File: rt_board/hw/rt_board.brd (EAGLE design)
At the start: 100 x 80 mm, 23 parts, among them IC1 MCP170333MB, IC2 FT232RL, Q1 8MHz, U1 STM32F051R8T7, X1 PWR, X2 MINI-USB

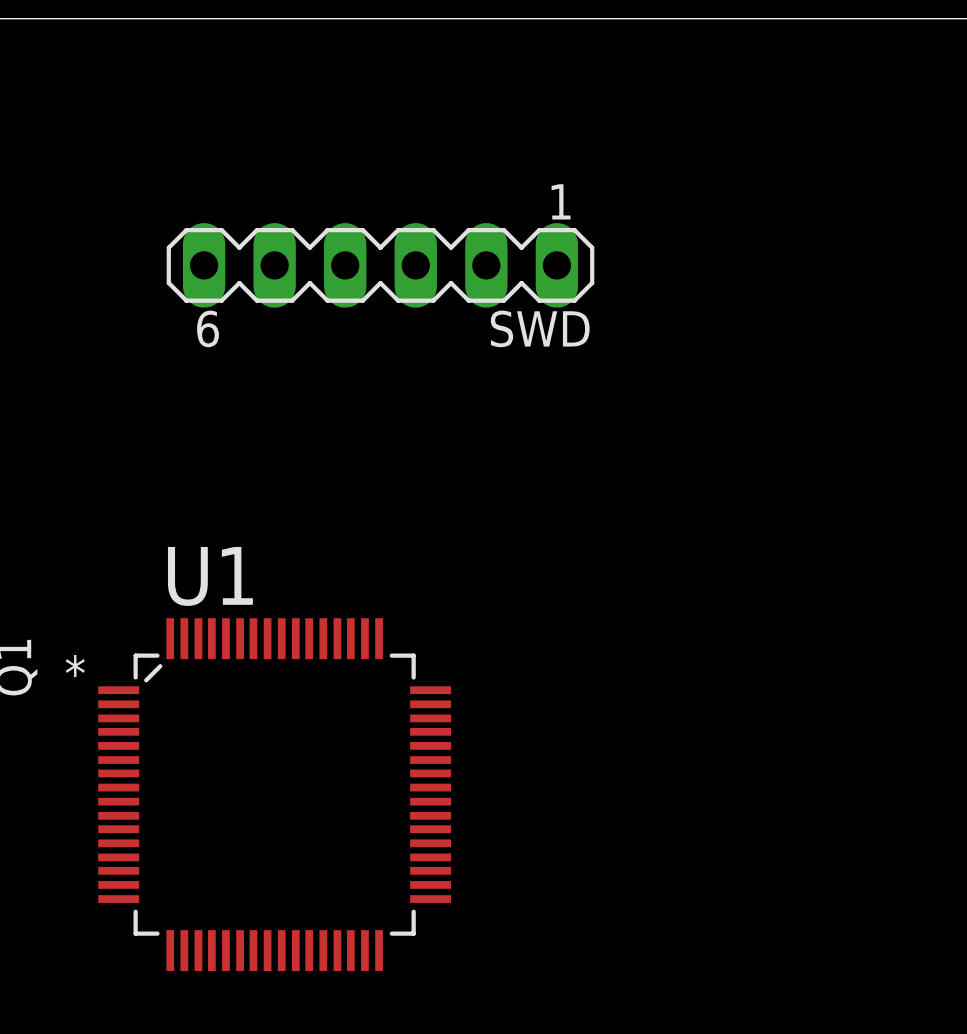
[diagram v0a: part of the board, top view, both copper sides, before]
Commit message: fixed SWD connection; added power VccIo to FT232
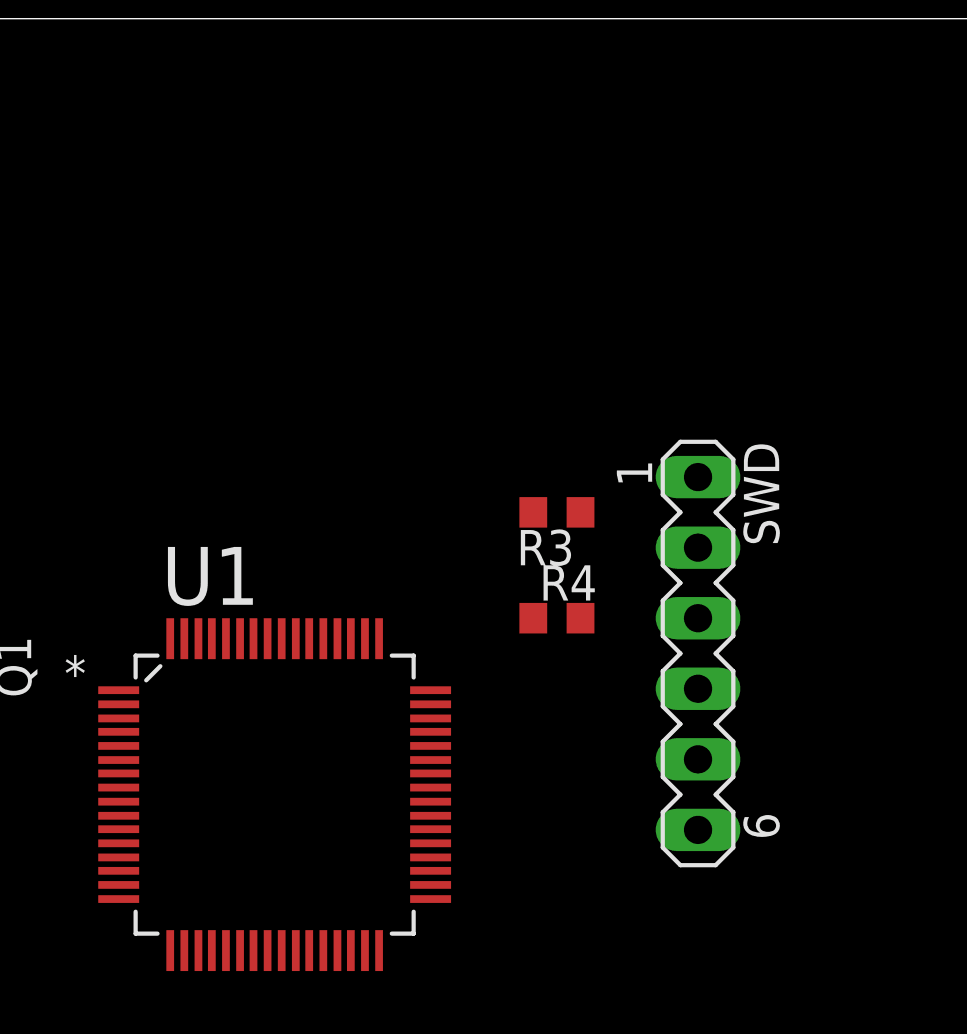
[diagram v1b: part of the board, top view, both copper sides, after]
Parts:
- added R3, R4: 100kR, rcl:R0603
- moved SWD 18.1 mm to (66.0, 57.1), turned to 270 degrees
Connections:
- removed net N$10: SWD.6, U1.55
- removed net VCCIO: IC2.4
- net +5V: now also R4.2, SWD.1
- net 0V: now also R3.1
- net N$13: now also IC2.4
- net N$4: now also R3.2
- net N$9: now also R4.1
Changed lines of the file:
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@@
 <element name="L1" library="rcl" package="L2012C" value="10uH" x="41.91" y="41.91" rot="R90"/>
 <element name="C10" library="rcl" package="C1206" value="100nF" x="46.99" y="40.64" rot="R270"/>
-<element name="SWD" library="con-lstb" package="MA06-1" value="" x="54.61" y="71.12" rot="R180">
-<attribute name="OC_NEWARK" value="unknown" x="54.61" y="71.12" size="1.778" layer="27" rot="R180" display="off"/>
-<attribute name="MPN" value="" x="54.61" y="71.12" size="1.778" layer="27" rot="R180" display="off"/>
-<attribute name="MF" value="" x="54.61" y="71.12" size="1.778" layer="27" rot="R180" display="off"/>
-<attribute name="OC_FARNELL" value="unknown" x="54.61" y="71.12" size="1.778" layer="27" rot="R180" display="off"/>
+<element name="SWD" library="con-lstb" package="MA06-1" value="" x="66.04" y="57.15" rot="R270">
+<attribute name="OC_NEWARK" value="unknown" x="66.04" y="57.15" size="1.778" layer="27" rot="R270" display="off"/>
+<attribute name="MPN" value="" x="66.04" y="57.15" size="1.778" layer="27" rot="R270" display="off"/>
+<attribute name="MF" value="" x="66.04" y="57.15" size="1.778" layer="27" rot="R270" display="off"/>
+<attribute name="OC_FARNELL" value="unknown" x="66.04" y="57.15" size="1.778" layer="27" rot="R270" display="off"/>
 </element>
 <element name="X2" library="con-cypressindustries" package="32005-201" value="MINI-USB" x="6.35" y="12.7">
@@
 </element>
 <element name="C11" library="rcl" package="C1206" value="100nF" x="17.78" y="6.35" rot="R180"/>
+<element name="R3" library="rcl" package="R0603" value="100kR" x="60.96" y="62.23" rot="R180"/>
+<element name="R4" library="rcl" package="R0603" value="100kR" x="60.96" y="58.42"/>
 </elements>
 <signals>
@@
 <contactref element="IC2" pad="26"/>
 <contactref element="C11" pad="2"/>
-<wire x1="47.5488" y1="57.6834" x2="55.88" y2="71.12" width="0" layer="19" extent="1-1"/>
+<contactref element="R3" pad="1"/>
+<wire x1="47.5488" y1="57.6834" x2="66.04" y2="58.42" width="0" layer="19" extent="1-1"/>
 <wire x1="45.1866" y1="50.3174" x2="47.5488" y2="57.6834" width="0" layer="19" extent="1-1"/>
 <wire x1="54.0512" y1="46.4566" x2="45.1866" y2="50.3174" width="0" layer="19" extent="1-1"/>
@@
 <wire x1="16.64" y1="17.78" x2="16.64" y2="22.86" width="0" layer="19" extent="1-1"/>
 <wire x1="16.64" y1="12.7" x2="16.64" y2="17.78" width="0" layer="19" extent="1-1"/>
+<wire x1="16.38" y1="6.35" x2="16.64" y2="12.7" width="0" layer="19" extent="1-1"/>
 <wire x1="23.045" y1="11.755" x2="16.64" y2="12.7" width="0" layer="19" extent="1-1"/>
 <wire x1="23.045" y1="13.705" x2="23.045" y2="11.755" width="0" layer="19" extent="1-1"/>
@@
 <wire x1="23.045" y1="8.505" x2="23.045" y2="9.155" width="0" layer="19" extent="1-1"/>
 <wire x1="30.295" y1="11.105" x2="23.045" y2="11.755" width="0" layer="19" extent="1-1"/>
-<wire x1="9.25" y1="17.15" x2="16.64" y2="17.78" width="0" layer="19" extent="1-1"/>
+<wire x1="9.25" y1="8.25" x2="16.38" y2="6.35" width="0" layer="19" extent="1-1"/>
+<wire x1="9.35" y1="11.1" x2="9.25" y2="8.25" width="0" layer="19" extent="1-1"/>
+<wire x1="3.35" y1="8.25" x2="9.25" y2="8.25" width="0" layer="19" extent="1-1"/>
+<wire x1="9.25" y1="17.15" x2="9.35" y2="11.1" width="0" layer="19" extent="1-1"/>
 <wire x1="3.35" y1="17.15" x2="9.25" y2="17.15" width="0" layer="19" extent="1-1"/>
-<wire x1="9.35" y1="11.1" x2="9.25" y2="17.15" width="0" layer="19" extent="1-1"/>
-<wire x1="9.25" y1="8.25" x2="9.35" y2="11.1" width="0" layer="19" extent="1-1"/>
-<wire x1="3.35" y1="8.25" x2="9.25" y2="8.25" width="0" layer="19" extent="1-1"/>
 <wire x1="10.9" y1="29.21" x2="16.64" y2="22.86" width="0" layer="19" extent="1-1"/>
+<wire x1="61.81" y1="62.23" x2="3.35" y2="8.25" width="0" layer="19" extent="1-1"/>
 <wire x1="7.46" y1="40.64" x2="10.9" y2="29.21" width="0" layer="19" extent="1-1"/>
-<wire x1="16.38" y1="6.35" x2="3.35" y2="8.25" width="0" layer="19" extent="1-1"/>
 <wire x1="3.81" y1="61.75" x2="7.46" y2="40.64" width="0" layer="19" extent="1-1"/>
 </signal>
@@
 <contactref element="U1" pad="32"/>
 <contactref element="L1" pad="1"/>
+<contactref element="SWD" pad="1"/>
+<contactref element="R4" pad="2"/>
+<wire x1="47.0408" y1="57.6834" x2="66.04" y2="63.5" width="0" layer="19" extent="1-1"/>
 <wire x1="45.1866" y1="55.8292" x2="47.0408" y2="57.6834" width="0" layer="19" extent="1-1"/>
 <wire x1="54.5592" y1="46.4566" x2="45.1866" y2="55.8292" width="0" layer="19" extent="1-1"/>
@@
 <wire x1="13.84" y1="12.7" x2="13.84" y2="17.78" width="0" layer="19" extent="1-1"/>
 <wire x1="27.2" y1="22.86" x2="23.28" y2="33.02" width="0" layer="19" extent="1-1"/>
+<wire x1="61.81" y1="58.42" x2="13.84" y2="12.7" width="0" layer="19" extent="1-1"/>
 </signal>
 <signal name="+12V">
@@
 <wire x1="3.81" y1="65.25" x2="2.9718" y2="73.66" width="0" layer="19" extent="1-1"/>
 </signal>
-<signal name="VCCIO">
-<contactref element="IC2" pad="4"/>
-</signal>
 <signal name="N$5">
 <contactref element="U1" pad="60"/>
@@
 <contactref element="C7" pad="1"/>
 <contactref element="SWD" pad="5"/>
-<wire x1="45.1866" y1="52.832" x2="50.8" y2="71.12" width="0" layer="19" extent="1-1"/>
+<wire x1="45.1866" y1="52.832" x2="66.04" y2="53.34" width="0" layer="19" extent="1-1"/>
 <wire x1="24.98" y1="33.02" x2="45.1866" y2="52.832" width="0" layer="19" extent="1-1"/>
 <wire x1="26.8" y1="29.21" x2="24.98" y2="33.02" width="0" layer="19" extent="1-1"/>
@@
 <contactref element="SWD" pad="2"/>
 <contactref element="U1" pad="49"/>
-<wire x1="54.5592" y1="57.6834" x2="58.42" y2="71.12" width="0" layer="19" extent="1-1"/>
+<contactref element="R3" pad="2"/>
+<wire x1="54.5592" y1="57.6834" x2="66.04" y2="60.96" width="0" layer="19" extent="1-1"/>
+<wire x1="60.11" y1="62.23" x2="54.5592" y2="57.6834" width="0" layer="19" extent="1-1"/>
 </signal>
 <signal name="N$9">
 <contactref element="U1" pad="46"/>
 <contactref element="SWD" pad="4"/>
-<wire x1="56.4134" y1="54.8132" x2="53.34" y2="71.12" width="0" layer="19" extent="1-1"/>
-</signal>
-<signal name="N$10">
-<contactref element="U1" pad="55"/>
-<contactref element="SWD" pad="6"/>
-<wire x1="51.562" y1="57.6834" x2="48.26" y2="71.12" width="0" layer="19" extent="1-1"/>
+<contactref element="R4" pad="1"/>
+<wire x1="56.4134" y1="54.8132" x2="66.04" y2="55.88" width="0" layer="19" extent="1-1"/>
+<wire x1="60.11" y1="58.42" x2="56.4134" y2="54.8132" width="0" layer="19" extent="1-1"/>
 </signal>
 <signal name="N$11">
@@
 <contactref element="IC2" pad="17"/>
 <contactref element="C11" pad="1"/>
+<contactref element="IC2" pad="4"/>
 <wire x1="19.18" y1="6.35" x2="23.045" y2="14.355" width="0" layer="19" extent="1-1"/>
+<wire x1="30.295" y1="9.155" x2="23.045" y2="14.355" width="0" layer="19" extent="1-1"/>
 </signal>
 </signals>

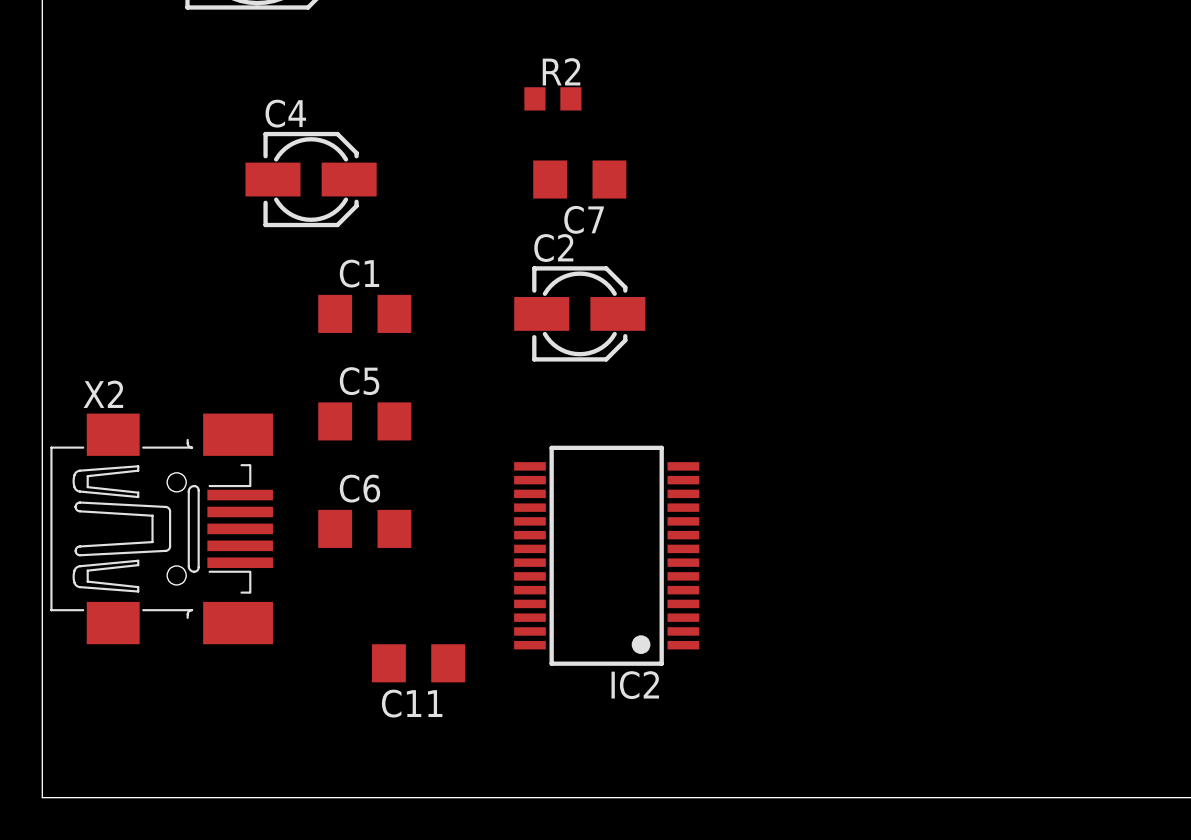
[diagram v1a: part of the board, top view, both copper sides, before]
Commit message: resigned from ft232 and USB communication in favor of direct communication with Panda's usart, via sn74avc4t245pw level converter
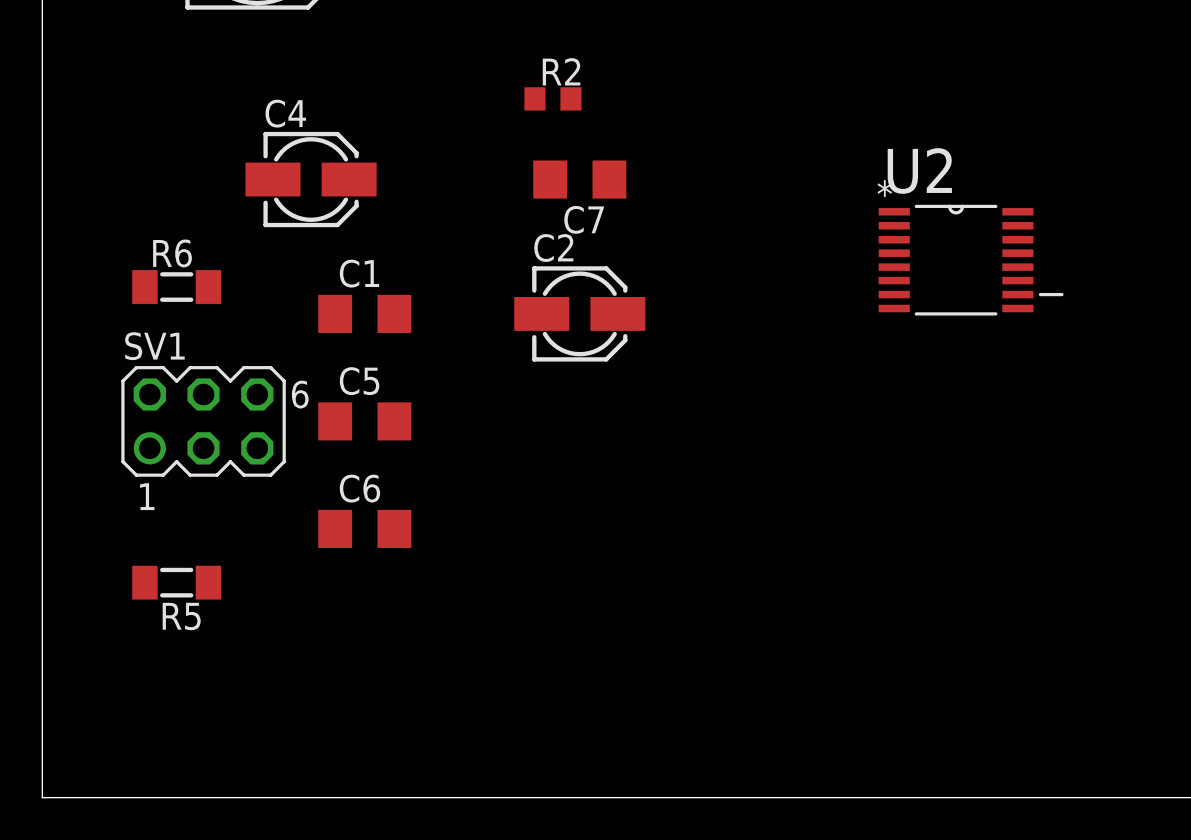
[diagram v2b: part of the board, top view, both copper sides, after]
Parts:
- removed C11: 100nF, rcl:C1206
- removed IC2: FT232RL, ftdichip:SSOP28
- removed X2: MINI-USB, con-cypressindustries:32005-201
- added R5, R6: 350mA, rcl:MINI_MELF-0204W
- added SV1: Panda J3, con-lstb:MA03-2
- added U2: SN74AVC4T245PW, TI-SN74AVC4T245PW:SOP65P640X120-16N
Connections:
- new net +5V/4: R5.1, U2.1, U2.2
- new net N$10: R6.1, SV1.2
- new net N$14: U1.16, U2.11
- new net N$15: SV1.4, U2.6
- net +12V: no longer D1.A
- net +5V: now also U2.16
- net +5V/1: now also D1.A, R6.2; no longer IC2.20, X2.1
- net 0V: now also SV1.5, SV1.6, U2.14, U2.15, U2.3, U2.8, U2.9; no longer C11.2, IC2.18, IC2.21, IC2.25, IC2.26, IC2.7, X2.5, X2.M1, X2.M2, X2.M3, X2.M4
- net N$11: now also R5.2, SV1.1; no longer IC2.16, X2.2
- net N$12: now also SV1.3, U2.4; no longer IC2.15, X2.3
- net N$13: now also U1.17, U2.13; no longer C11.1, IC2.17, IC2.4
